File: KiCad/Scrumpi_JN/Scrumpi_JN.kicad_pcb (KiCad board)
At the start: 4 copper layers, 165.1 x 127 mm, 203 parts

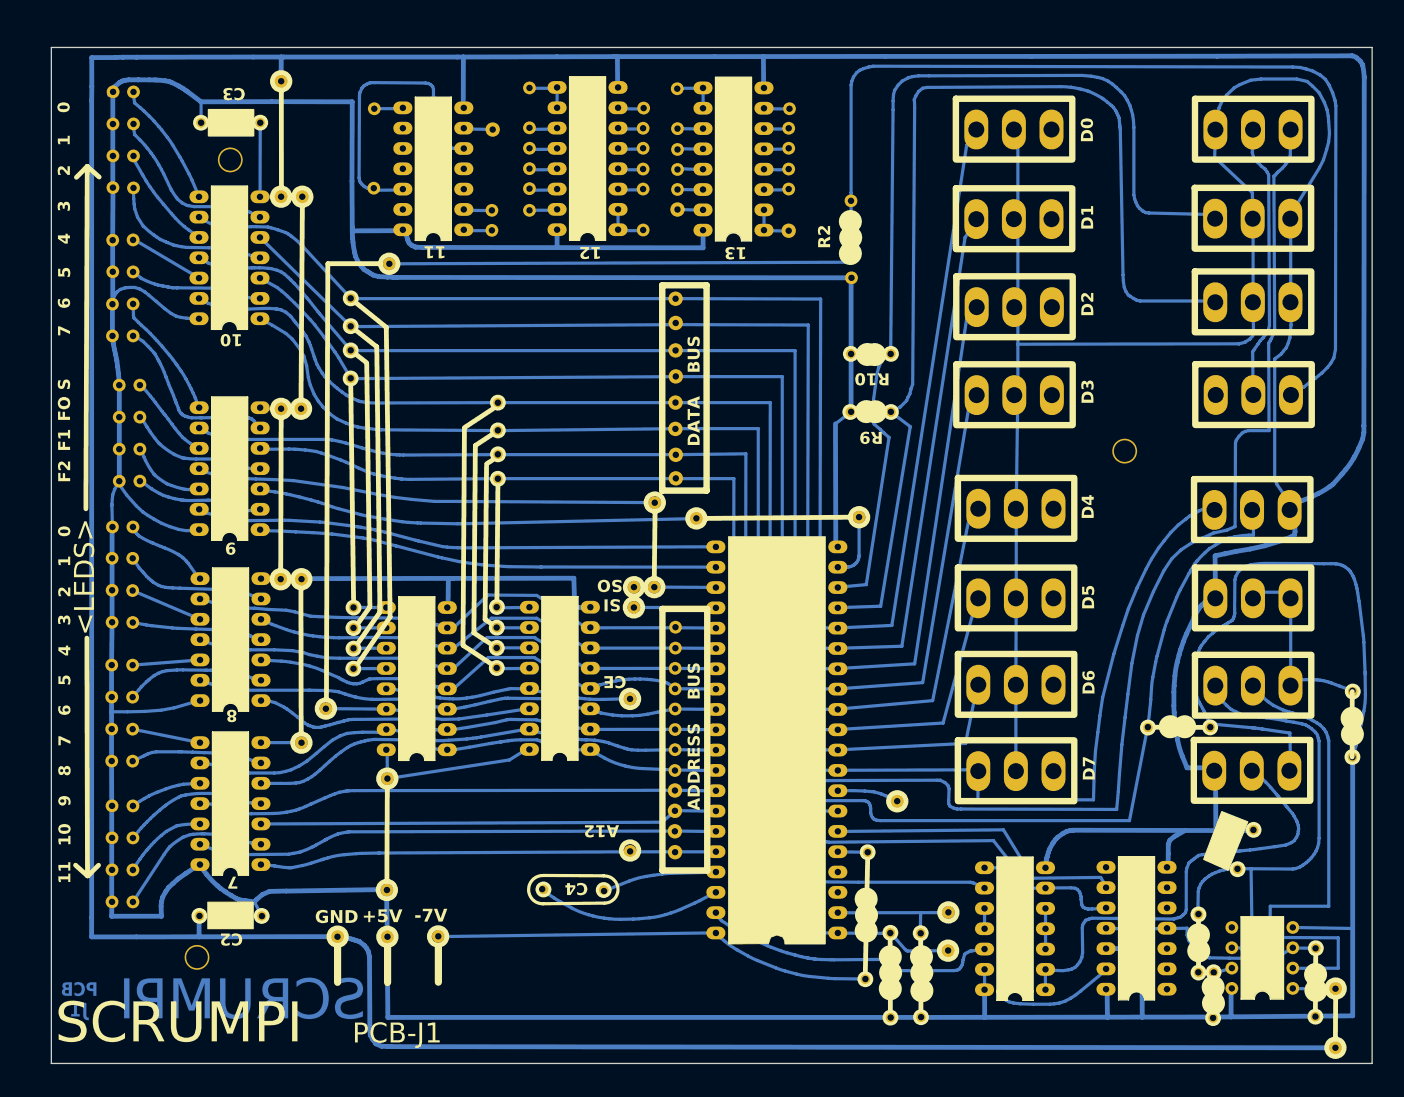
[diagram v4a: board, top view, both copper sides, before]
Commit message: Resized the board.
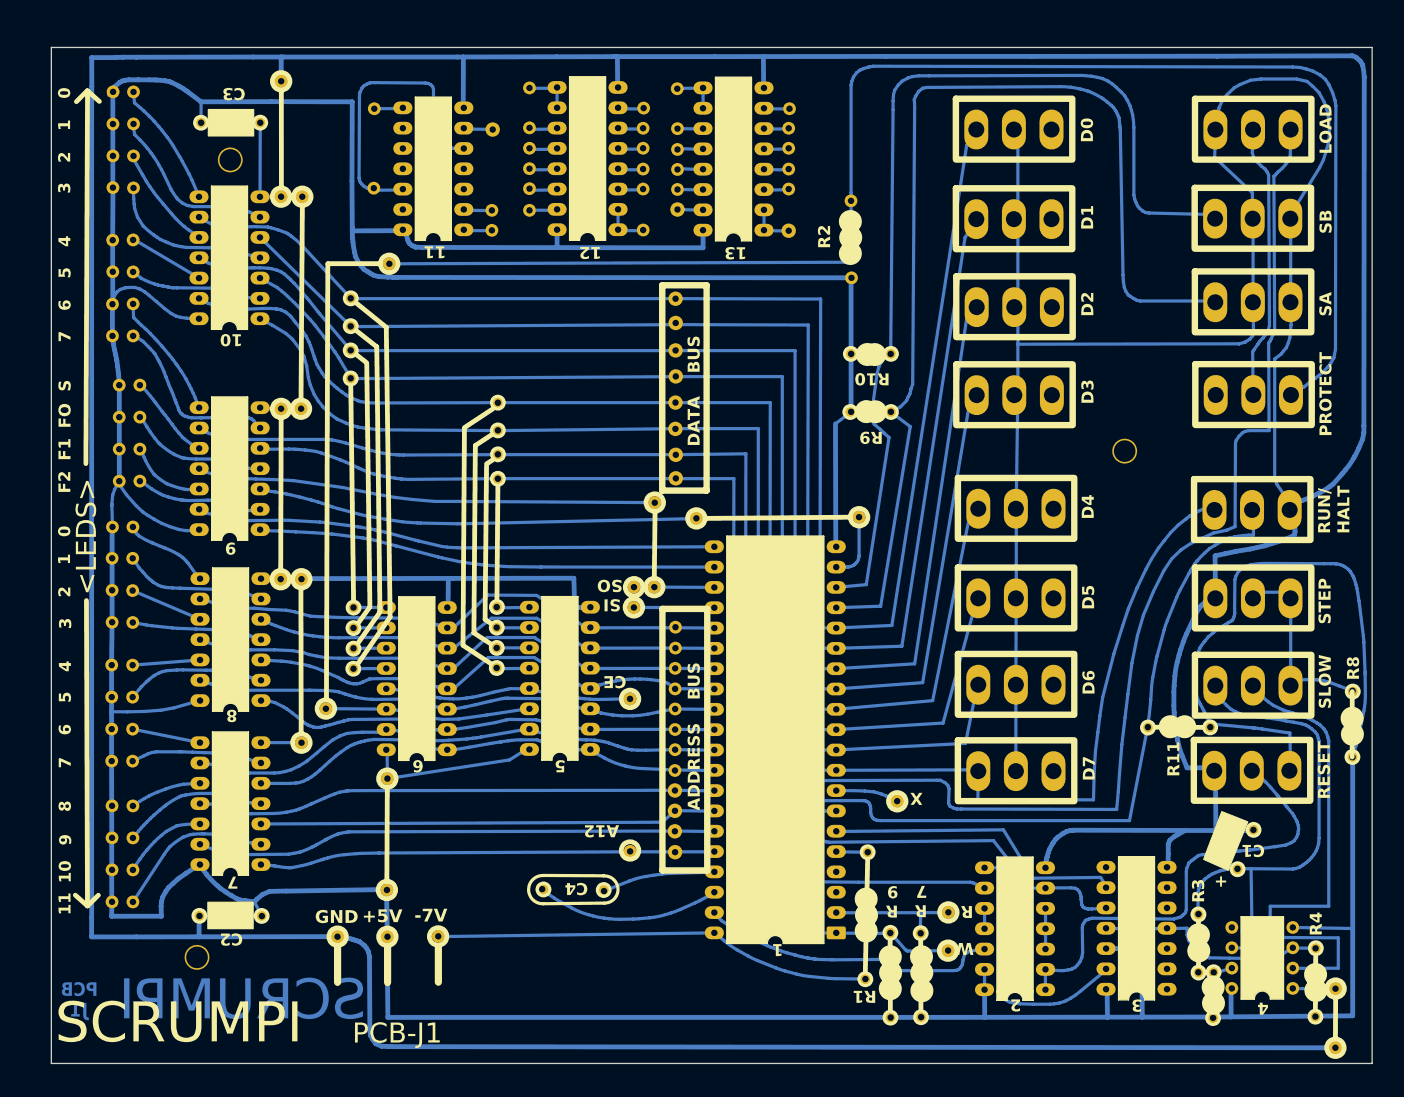
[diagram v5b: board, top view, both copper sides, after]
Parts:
- REF**: moved to F.Cu
- moved REF** 15.0 mm to (173.9, 136.8), turned to 180 degrees
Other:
- board text added: "+"
- board text added: "C1"
- board text added: "LOAD"
- board text added: "PROTECT"
- board text added: "R"
- board text added: "R 7"
- board text added: "R 9"
- board text added: "R1"
- board text added: "R11"
- board text added: "R3"
- board text added: "R4"
- board text added: "R8"
- board text added: "RESET"
- board text added: "RUN/ HALT"
- board text added: "SA"
- board text added: "SB"
- board text added: "SLOW"
- board text added: "STEP"
- board text added: "W"
- board text added: "X"
